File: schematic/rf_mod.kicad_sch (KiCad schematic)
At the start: 32 parts, among them J4A1 Conn_01x08, Q3 2N3906, Q6 2N3906, U23 4066

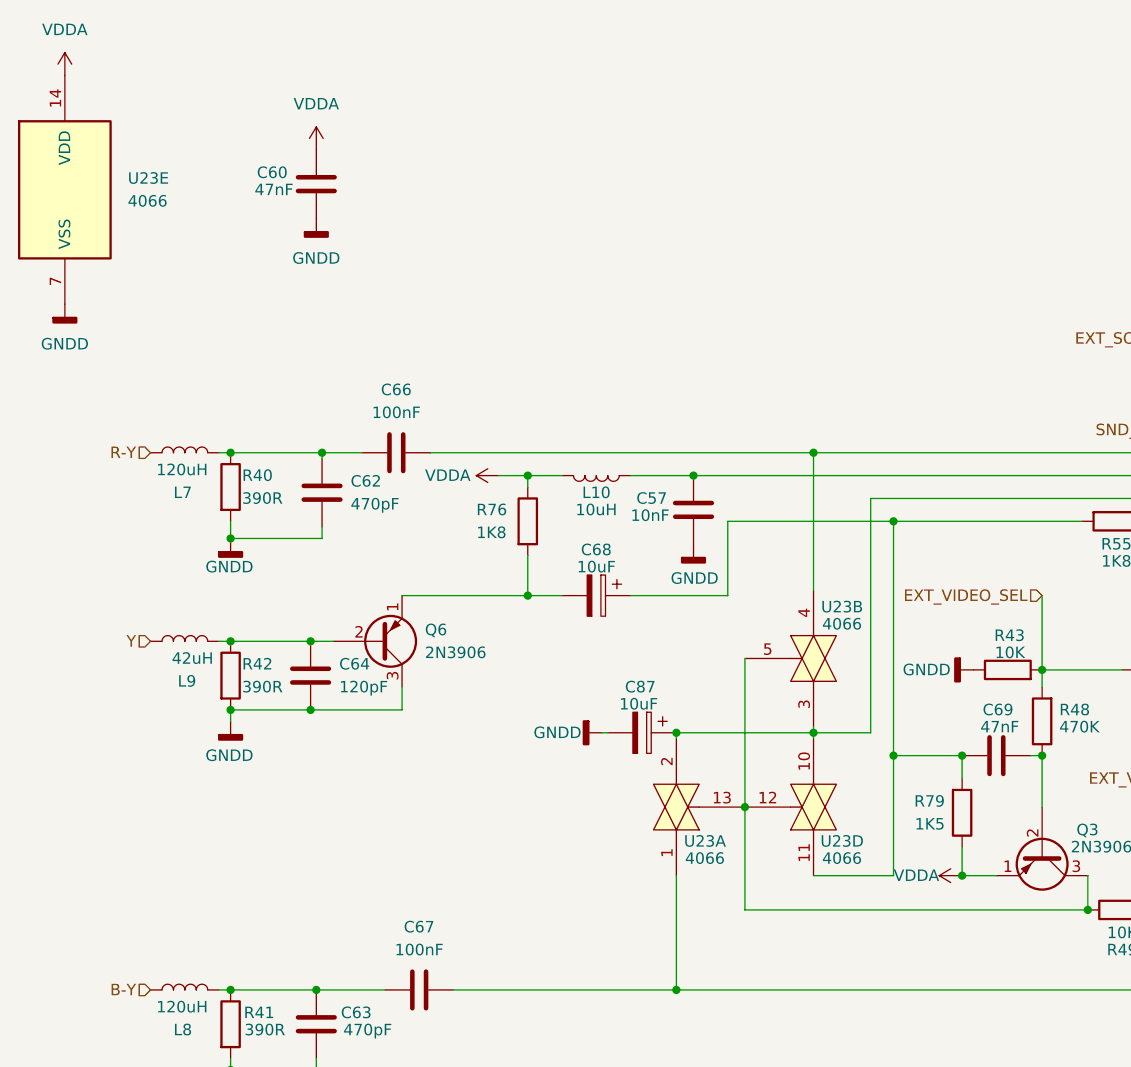
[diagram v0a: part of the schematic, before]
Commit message: added traces to parts of the clock gen/reset ic's
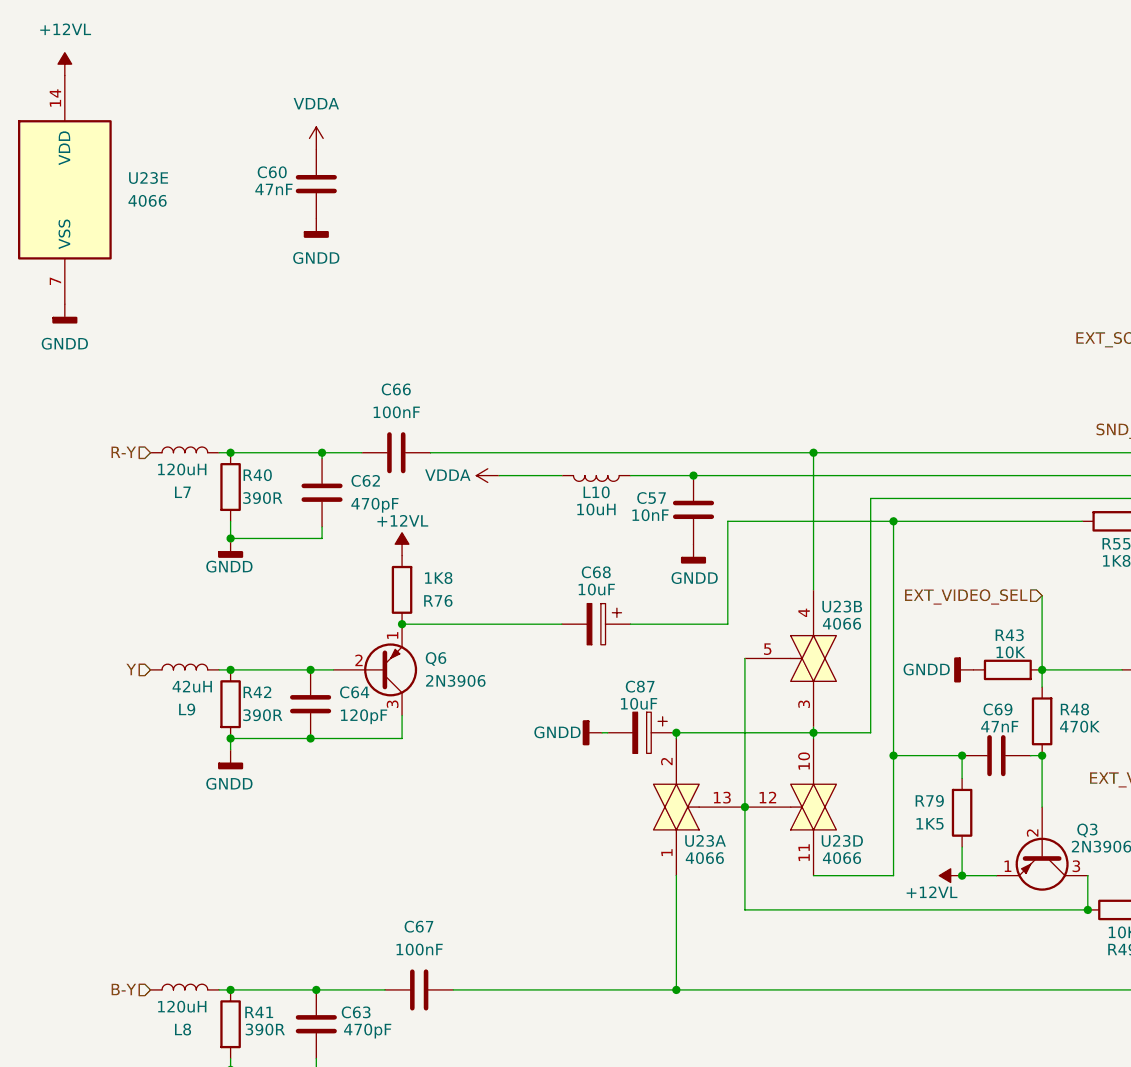
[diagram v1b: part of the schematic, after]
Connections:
- net VDDA: no longer Q3.1 (E), R76.1, R79.1, U23.14 (VDD)
- net at C68.2, Q6.1 (E): now also R76.1; no longer R76.2
- new net +12VL: Q3.1 (E), R76.2, R79.1, U23.14 (VDD)
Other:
- moved on the sheet: C64, C68, L9, Q6, R42, R76

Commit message: added memory, eprom and sound lines. some video as well. fixed the cap size for polar. its a bit weird since they use 5 mm pin and 5mm body and bend out the leads.
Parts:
- C68, C87: footprint Capacitor_THT:CP_Radial_D5.0mm_P2.50mm -> Capacitor_THT:CP_Radial_Tantal_D4.5mm_P5.00mm
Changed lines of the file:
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@@
     (property "Reference" "C68" (id 0) (at 98.425 79.375 90))
     (property "Value" "10uF" (id 1) (at 98.425 81.28 90))
-    (property "Footprint" "Capacitor_THT:CP_Radial_D5.0mm_P2.50mm" (id 2) (at 94.615 86.0552 0)
+    (property "Footprint" "Capacitor_THT:CP_Radial_Tantal_D4.5mm_P5.00mm" (id 2) (at 94.615 86.0552 0)
       (effects (font (size 1.27 1.27)) hide)
     )
@@
       (effects (font (size 1.27 1.27)) (justify left))
     )
-    (property "Footprint" "Capacitor_THT:CP_Radial_D5.0mm_P2.50mm" (id 2) (at 99.695 98.1202 0)
-      (effects (font (size 1.27 1.27)) hide)
-    )
+    (property "Footprint" "Capacitor_THT:CP_Radial_Tantal_D4.5mm_P5.00mm" (id 2) (at 99.695 98.1202 0)
+      (effects (font (size 1.27 1.27)) hide)
+    )

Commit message: added new models, fixed the drc errors. changed power width.
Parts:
- C68, C87: footprint Capacitor_THT:CP_Radial_Tantal_D4.5mm_P5.00mm -> Capacitor_THT:CP_Radial_D8.0mm_P5.00mm
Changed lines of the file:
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@@
     (property "Reference" "C68" (id 0) (at 98.425 79.375 90))
     (property "Value" "10uF" (id 1) (at 98.425 81.28 90))
-    (property "Footprint" "Capacitor_THT:CP_Radial_Tantal_D4.5mm_P5.00mm" (id 2) (at 94.615 86.0552 0)
+    (property "Footprint" "Capacitor_THT:CP_Radial_D8.0mm_P5.00mm" (id 2) (at 94.615 86.0552 0)
       (effects (font (size 1.27 1.27)) hide)
     )
@@
       (effects (font (size 1.27 1.27)) (justify left))
     )
-    (property "Footprint" "Capacitor_THT:CP_Radial_Tantal_D4.5mm_P5.00mm" (id 2) (at 99.695 98.1202 0)
-      (effects (font (size 1.27 1.27)) hide)
-    )
+    (property "Footprint" "Capacitor_THT:CP_Radial_D8.0mm_P5.00mm" (id 2) (at 99.695 98.1202 0)
+      (effects (font (size 1.27 1.27)) hide)
+    )

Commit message: updated schematic with new layout
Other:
- company: (none) -> sparkletron
- title: Colecovision Schematic -> Reverse Engineer Colecovision
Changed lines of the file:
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@@
   (paper "USLetter")
   (title_block
-    (title "Colecovision Schematic")
-    (date "2023-01-09")
-    (rev "F.0")
+    (title "Reverse Engineer Colecovision")
+    (date "2023-03-14")
+    (rev "DEV")
+    (company "sparkletron")
     (comment 1 "Jay Convertino")
+    (comment 2 "MIT LICENSE")
   )
   (junction (at 147.955 99.695) (diameter 0) (color 0 0 0 0)

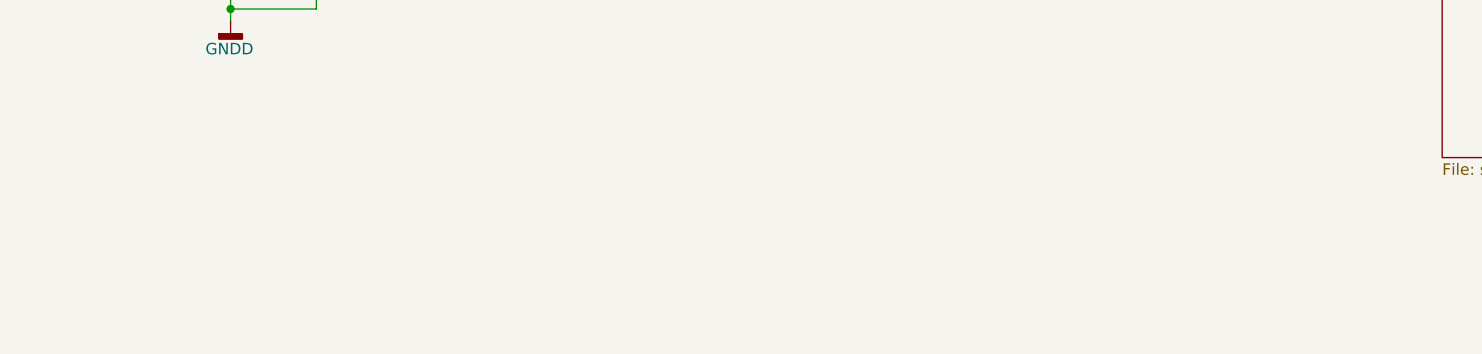
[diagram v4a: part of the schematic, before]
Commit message: added pads for switch and RF shield, RF shield still needs adjustment
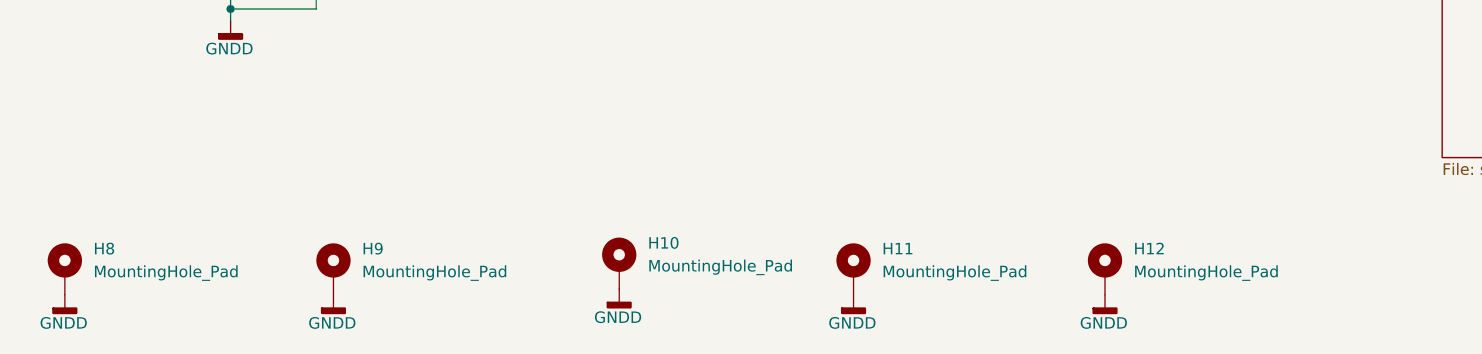
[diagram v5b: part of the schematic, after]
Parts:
- added H10, H11, H12, H8, H9: MountingHole_Pad, mount_points:RF_MOUNT, symbol Mechanical:MountingHole_Pad
- C87: footprint Capacitor_THT:CP_Radial_D8.0mm_P5.00mm -> Capacitor_THT:CP_Radial_D5.0mm_P2.50mm
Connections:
- net GNDD: now also H10.1, H11.1, H12.1, H8.1, H9.1
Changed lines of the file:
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@@
     (pin "2")
+  )
+  (symbol (lib_id "power:GNDD") (at 127 166.37 0) (unit 1)
+    (in_bom yes) (on_board yes)
+    (property "Reference" "#PWR0280" (id 0) (at 127 172.72 0)
+      (effects (font (size 1.27 1.27)) hide)
+    )
+    (property "Value" "GNDD" (id 1) (at 129.54 169.545 0)
+      (effects (font (size 1.27 1.27)) (justify right))
+    )
+    (property "Footprint" "" (id 2) (at 127 166.37 0)
+      (effects (font (size 1.27 1.27)) hide)
+    )
+    (property "Datasheet" "" (id 3) (at 127 166.37 0)
+      (effects (font (size 1.27 1.27)) hide)
+    )
+    (pin "1")
+  )
+  (symbol (lib_id "power:GNDD") (at 100.965 165.735 0) (unit 1)
+    (in_bom yes) (on_board yes)
+    (property "Reference" "#PWR0277" (id 0) (at 100.965 172.085 0)
+      (effects (font (size 1.27 1.27)) hide)
+    )
+    (property "Value" "GNDD" (id 1) (at 103.505 168.91 0)
+      (effects (font (size 1.27 1.27)) (justify right))
+    )
+    (property "Footprint" "" (id 2) (at 100.965 165.735 0)
+      (effects (font (size 1.27 1.27)) hide)
+    )
+    (property "Datasheet" "" (id 3) (at 100.965 165.735 0)
+      (effects (font (size 1.27 1.27)) hide)
+    )
+    (pin "1")
   )
   (symbol (lib_id "4xxx:4066") (at 122.555 88.9 90) (mirror x) (unit 2)
@@
     (pin "2")
   )
+  (symbol (lib_id "power:GNDD") (at 69.215 166.37 0) (unit 1)
+    (in_bom yes) (on_board yes)
+    (property "Reference" "#PWR0279" (id 0) (at 69.215 172.72 0)
+      (effects (font (size 1.27 1.27)) hide)
+    )
+    (property "Value" "GNDD" (id 1) (at 71.755 169.545 0)
+      (effects (font (size 1.27 1.27)) (justify right))
+    )
+    (property "Footprint" "" (id 2) (at 69.215 166.37 0)
+      (effects (font (size 1.27 1.27)) hide)
+    )
+    (property "Datasheet" "" (id 3) (at 69.215 166.37 0)
+      (effects (font (size 1.27 1.27)) hide)
+    )
+    (pin "1")
+  )
+  (symbol (lib_id "Mechanical:MountingHole_Pad") (at 127 163.83 0) (unit 1)
+    (in_bom yes) (on_board yes) (fields_autoplaced)
+    (property "Reference" "H11" (id 0) (at 130.175 161.2899 0)
+      (effects (font (size 1.27 1.27)) (justify left))
+    )
+    (property "Value" "MountingHole_Pad" (id 1) (at 130.175 163.8299 0)
+      (effects (font (size 1.27 1.27)) (justify left))
+    )
+    (property "Footprint" "mount_points:RF_MOUNT" (id 2) (at 127 163.83 0)
+      (effects (font (size 1.27 1.27)) hide)
+    )
+    (property "Datasheet" "~" (id 3) (at 127 163.83 0)
+      (effects (font (size 1.27 1.27)) hide)
+    )
+    (pin "1")
+  )
+  (symbol (lib_id "power:GNDD") (at 39.37 166.37 0) (unit 1)
+    (in_bom yes) (on_board yes)
+    (property "Reference" "#PWR0278" (id 0) (at 39.37 172.72 0)
+      (effects (font (size 1.27 1.27)) hide)
+    )
+    (property "Value" "GNDD" (id 1) (at 41.91 169.545 0)
+      (effects (font (size 1.27 1.27)) (justify right))
+    )
+    (property "Footprint" "" (id 2) (at 39.37 166.37 0)
+      (effects (font (size 1.27 1.27)) hide)
+    )
+    (property "Datasheet" "" (id 3) (at 39.37 166.37 0)
+      (effects (font (size 1.27 1.27)) hide)
+    )
+    (pin "1")
+  )
   (symbol (lib_id "Device:C") (at 109.22 72.39 0) (mirror y) (unit 1)
     (in_bom yes) (on_board yes)
@@
     (pin "1")
   )
+  (symbol (lib_id "Mechanical:MountingHole_Pad") (at 69.215 163.83 0) (unit 1)
+    (in_bom yes) (on_board yes) (fields_autoplaced)
+    (property "Reference" "H9" (id 0) (at 72.39 161.2899 0)
+      (effects (font (size 1.27 1.27)) (justify left))
+    )
+    (property "Value" "MountingHole_Pad" (id 1) (at 72.39 163.8299 0)
+      (effects (font (size 1.27 1.27)) (justify left))
+    )
+    (property "Footprint" "mount_points:RF_MOUNT" (id 2) (at 69.215 163.83 0)
+      (effects (font (size 1.27 1.27)) hide)
+    )
+    (property "Datasheet" "~" (id 3) (at 69.215 163.83 0)
+      (effects (font (size 1.27 1.27)) hide)
+    )
+    (pin "1")
+  )
   (symbol (lib_id "Device:C") (at 67.31 36.195 0) (unit 1)
     (in_bom yes) (on_board yes)
@@
       (effects (font (size 1.27 1.27)) (justify left))
     )
-    (property "Footprint" "Capacitor_THT:CP_Radial_D8.0mm_P5.00mm" (id 2) (at 99.695 98.1202 0)
+    (property "Footprint" "Capacitor_THT:CP_Radial_D5.0mm_P2.50mm" (id 2) (at 99.695 98.1202 0)
       (effects (font (size 1.27 1.27)) hide)
     )
@@
     (pin "2")
     (pin "3")
+  )
+  (symbol (lib_id "Mechanical:MountingHole_Pad") (at 39.37 163.83 0) (unit 1)
+    (in_bom yes) (on_board yes) (fields_autoplaced)
+    (property "Reference" "H8" (id 0) (at 42.545 161.2899 0)
+      (effects (font (size 1.27 1.27)) (justify left))
+    )
+    (property "Value" "MountingHole_Pad" (id 1) (at 42.545 163.8299 0)
+      (effects (font (size 1.27 1.27)) (justify left))
+    )
+    (property "Footprint" "mount_points:RF_MOUNT" (id 2) (at 39.37 163.83 0)
+      (effects (font (size 1.27 1.27)) hide)
+    )
+    (property "Datasheet" "~" (id 3) (at 39.37 163.83 0)
+      (effects (font (size 1.27 1.27)) hide)
+    )
+    (pin "1")
   )
   (symbol (lib_id "power:GNDD") (at 39.37 49.53 0) (unit 1)
@@
     (pin "7")
   )
+  (symbol (lib_id "power:GNDD") (at 154.94 166.37 0) (unit 1)
+    (in_bom yes) (on_board yes)
+    (property "Reference" "#PWR0281" (id 0) (at 154.94 172.72 0)
+      (effects (font (size 1.27 1.27)) hide)
+    )
+    (property "Value" "GNDD" (id 1) (at 157.48 169.545 0)
+      (effects (font (size 1.27 1.27)) (justify right))
+    )
+    (property "Footprint" "" (id 2) (at 154.94 166.37 0)
+      (effects (font (size 1.27 1.27)) hide)
+    )
+    (property "Datasheet" "" (id 3) (at 154.94 166.37 0)
+      (effects (font (size 1.27 1.27)) hide)
+    )
+    (pin "1")
+  )
+  (symbol (lib_id "Mechanical:MountingHole_Pad") (at 100.965 163.195 0) (unit 1)
+    (in_bom yes) (on_board yes) (fields_autoplaced)
+    (property "Reference" "H10" (id 0) (at 104.14 160.6549 0)
+      (effects (font (size 1.27 1.27)) (justify left))
+    )
+    (property "Value" "MountingHole_Pad" (id 1) (at 104.14 163.1949 0)
+      (effects (font (size 1.27 1.27)) (justify left))
+    )
+    (property "Footprint" "mount_points:RF_MOUNT" (id 2) (at 100.965 163.195 0)
+      (effects (font (size 1.27 1.27)) hide)
+    )
+    (property "Datasheet" "~" (id 3) (at 100.965 163.195 0)
+      (effects (font (size 1.27 1.27)) hide)
+    )
+    (pin "1")
+  )
+  (symbol (lib_id "Mechanical:MountingHole_Pad") (at 154.94 163.83 0) (unit 1)
+    (in_bom yes) (on_board yes) (fields_autoplaced)
+    (property "Reference" "H12" (id 0) (at 158.115 161.2899 0)
+      (effects (font (size 1.27 1.27)) (justify left))
+    )
+    (property "Value" "MountingHole_Pad" (id 1) (at 158.115 163.8299 0)
+      (effects (font (size 1.27 1.27)) (justify left))
+    )
+    (property "Footprint" "mount_points:RF_MOUNT" (id 2) (at 154.94 163.83 0)
+      (effects (font (size 1.27 1.27)) hide)
+    )
+    (property "Datasheet" "~" (id 3) (at 154.94 163.83 0)
+      (effects (font (size 1.27 1.27)) hide)
+    )
+    (pin "1")
+  )
   (symbol (lib_id "Transistor_BJT:2N3906") (at 74.295 90.17 0) (mirror x) (unit 1)
